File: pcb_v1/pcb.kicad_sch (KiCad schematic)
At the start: 137 parts, among them SW1 RotaryEncoder

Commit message: Added Flex Cuts
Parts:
- removed SW1: RotaryEncoder, My_Footprints:EN05VS1212NHH, symbol Device:RotaryEncoder

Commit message: Wiring Update
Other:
- moved on the sheet: D1, D10, D11, D12, D13, D14, D15, D16, D17, D18, D19, D2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

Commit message: Changed Layout of Keyboard
Row 1, Column 14 Removed due to OLED Screen taking up 2x2 u space
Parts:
- removed D29: D_Small, ScottoKeebs_Components:Diode_SOD-123, symbol Device:D_Small
- removed S29: Keyswitch, PCM_marbastlib-mx:SW_MX_HS_CPG151101S11_1u, symbol ScottoKeebs:Placeholder_Keyswitch
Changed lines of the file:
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@@
 	)
 	(junction
-		(at 223.52 83.82)
-		(diameter 0)
-		(color 0 0 0 0)
-	)
-	(junction
 		(at 104.14 73.66)
 		(diameter 0)
@@
 	)
 	(junction
-		(at 218.44 73.66)
-		(diameter 0)
-		(color 0 0 0 0)
-	)
-	(junction
 		(at 200.66 67.31)
 		(diameter 0)
@@
 	(wire
 		(pts
-			(xy 223.52 83.82) (xy 236.22 83.82)
-		)
-		(stroke
-			(width 0)
-			(type default)
-		)
-	)
-	(wire
-		(pts
 			(xy 58.42 57.15) (xy 58.42 73.66)
 		)
@@
 	(wire
 		(pts
-			(xy 218.44 73.66) (xy 218.44 90.17)
-		)
-		(stroke
-			(width 0)
-			(type default)
-		)
-	)
-	(wire
-		(pts
 			(xy 86.36 83.82) (xy 97.79 83.82)
 		)
@@
 	(wire
 		(pts
-			(xy 218.44 45.72) (xy 218.44 73.66)
+			(xy 218.44 45.72) (xy 218.44 90.17)
 		)
 		(stroke
@@
 	(wire
 		(pts
-			(xy 212.09 83.82) (xy 223.52 83.82)
+			(xy 212.09 83.82) (xy 236.22 83.82)
 		)
 		(stroke
@@
 	(symbol
 		(lib_id "Device:D_Small")
-		(at 223.52 81.28 90)
-		(unit 1)
-		(exclude_from_sim no)
-		(in_bom yes)
-		(on_board yes)
-		(dnp no)
-		(fields_autoplaced yes)
-		(property "Reference" "D29"
-			(at 226.06 80.0099 90)
-			(effects
-				(font
-					(size 1.27 1.27)
-				)
-				(justify right)
-			)
-		)
-		(property "Value" "D_Small"
-			(at 226.06 82.5499 90)
-			(effects
-				(font
-					(size 1.27 1.27)
-				)
-				(justify right)
-			)
-		)
-		(property "Footprint" "ScottoKeebs_Components:Diode_SOD-123"
-			(at 223.52 81.28 90)
-			(effects
-				(font
-					(size 1.27 1.27)
-				)
-				(hide yes)
-			)
-		)
-		(property "Datasheet" "~"
-			(at 223.52 81.28 90)
-			(effects
-				(font
-					(size 1.27 1.27)
-				)
-				(hide yes)
-			)
-		)
-		(property "Description" "Diode, small symbol"
-			(at 223.52 81.28 0)
-			(effects
-				(font
-					(size 1.27 1.27)
-				)
-				(hide yes)
-			)
-		)
-		(property "Sim.Device" "D"
-			(at 223.52 81.28 0)
-			(effects
-				(font
-					(size 1.27 1.27)
-				)
-				(hide yes)
-			)
-		)
-		(property "Sim.Pins" "1=K 2=A"
-			(at 223.52 81.28 0)
-			(effects
-				(font
-					(size 1.27 1.27)
-				)
-				(hide yes)
-			)
-		)
-		(pin "1"
-		)
-		(pin "2"
-		)
-		(instances
-			(project "pcb_v1"
-				(path "/bf36a815-88b9-4f95-84c3-6b01513341e6/a99efd52-74f7-4830-b1d0-0b8eae050ef9"
-					(reference "D29")
-					(unit 1)
-				)
-			)
-		)
-	)
-	(symbol
-		(lib_id "Device:D_Small")
 		(at 200.66 81.28 90)
 		(unit 1)
@@
 					(unit 1)
 				)
-			)
-		)
-	)
-	(symbol
-		(lib_id "ScottoKeebs:Placeholder_Keyswitch")
-		(at 220.98 76.2 0)
-		(unit 1)
-		(exclude_from_sim no)
-		(in_bom yes)
-		(on_board yes)
-		(dnp no)
-		(fields_autoplaced yes)
-		(property "Reference" "S29"
-			(at 220.98 68.58 0)
-			(effects
-				(font
-					(size 1.27 1.27)
-				)
-			)
-		)
-		(property "Value" "Keyswitch"
-			(at 220.98 71.12 0)
-			(effects
-				(font
-					(size 1.27 1.27)
-				)
-			)
-		)
-		(property "Footprint" "PCM_marbastlib-mx:SW_MX_HS_CPG151101S11_1u"
-			(at 220.98 76.2 0)
-			(effects
-				(font
-					(size 1.27 1.27)
-				)
-				(hide yes)
-			)
-		)
-		(property "Datasheet" "~"
-			(at 220.98 76.2 0)
-			(effects
-				(font
-					(size 1.27 1.27)
-				)
-				(hide yes)
-			)
-		)
-		(property "Description" "Push button switch, normally open, two pins, 45° tilted"
-			(at 220.98 76.2 0)
-			(effects
-				(font
-					(size 1.27 1.27)
-				)
-				(hide yes)
-			)
-		)
-		(pin "1"
-		)
-		(pin "2"
-		)
-		(instances
-			(project "pcb_v1"
-				(path "/bf36a815-88b9-4f95-84c3-6b01513341e6/a99efd52-74f7-4830-b1d0-0b8eae050ef9"
-					(reference "S29")
-					(unit 1)
-				)

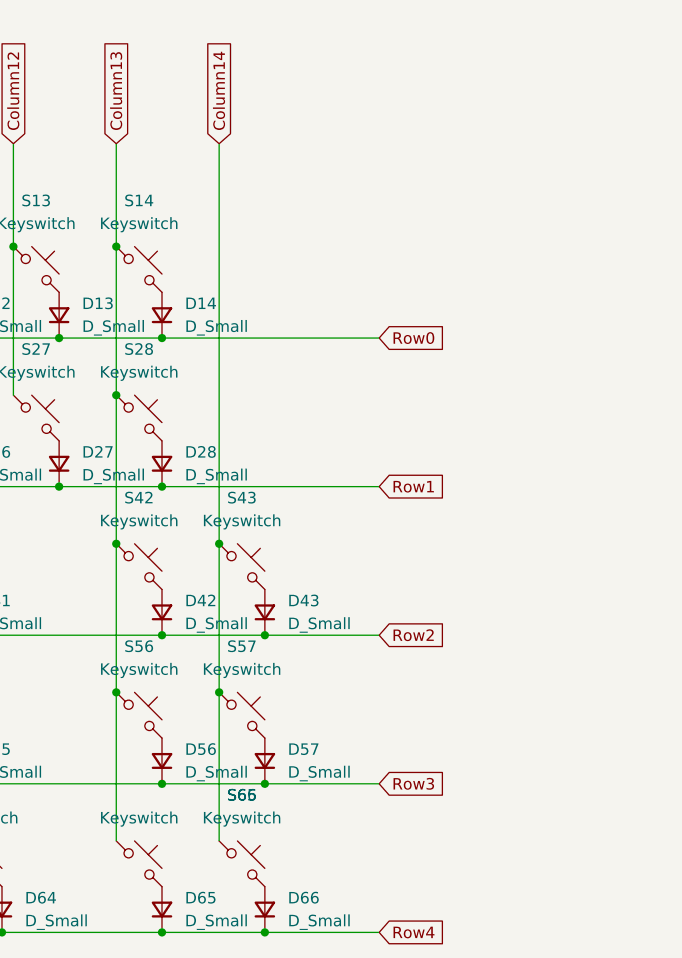
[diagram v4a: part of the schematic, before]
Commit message: Changed PCB to Accommodate Revised Layout
Added a few more keys to balance the screen being 2u x 2u, therefore extending the length of the PCB
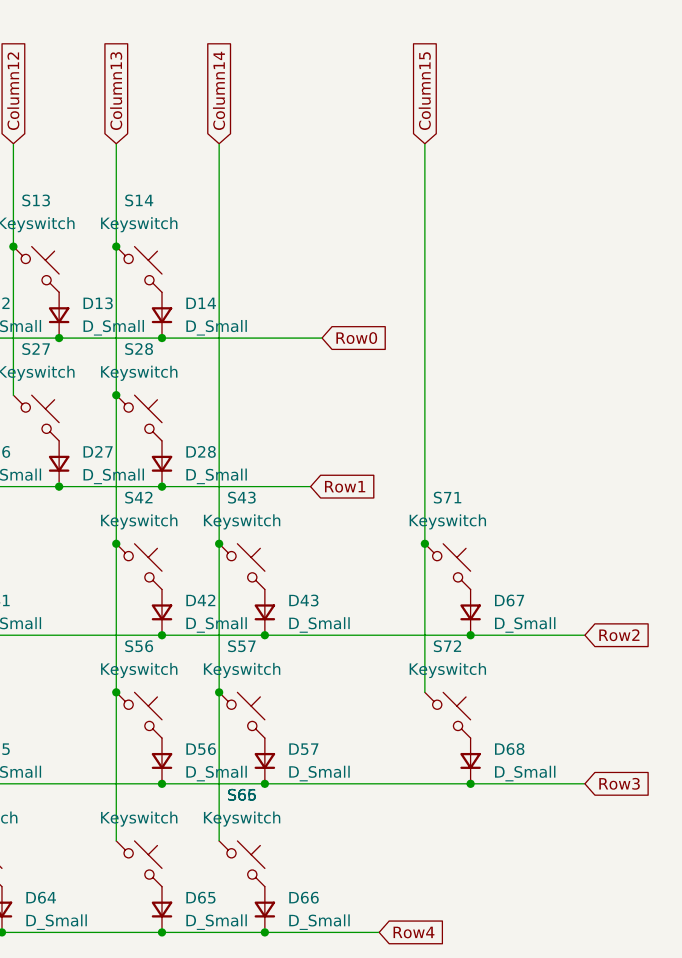
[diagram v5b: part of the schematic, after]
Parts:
- added D67, D68: D_Small, ScottoKeebs_Components:Diode_SOD-123, symbol Device:D_Small
- added S71, S72: Keyswitch, PCM_marbastlib-mx:SW_MX_HS_CPG151101S11_1u, symbol ScottoKeebs:Placeholder_Keyswitch
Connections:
- net Row2: now also D67.1 (K)
- net Row3: now also D68.1 (K)
- new net: D67.2 (A), S71.2
- new net: D68.2 (A), S72.2
- new net Column15: S71.1, S72.1
